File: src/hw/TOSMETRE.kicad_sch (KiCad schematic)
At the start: 61 parts

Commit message: #402
BROULLION
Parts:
- C1, C4: value (none) -> 1µF; footprint (none) -> Capacitor_SMD:C_1206_3216Metric
- C10, C13, C16, C3, C8: value (none) -> 100nF; footprint (none) -> Capacitor_SMD:C_1206_3216Metric
- C11: value (none) -> 2.2µF; footprint (none) -> Capacitor_SMD:C_1206_3216Metric
- C12, C5: value (none) -> 47nF; footprint (none) -> Capacitor_SMD:C_1206_3216Metric
- C14, C17, C2, C7, C9: value (none) -> 10µF; footprint (none) -> Capacitor_SMD:C_1206_3216Metric
- C15, C18: value (none) -> 2nF; footprint (none) -> Capacitor_SMD:C_1206_3216Metric
- C19, C20, C21, C22: value (none) -> NM; footprint (none) -> Capacitor_SMD:C_1206_3216Metric
- C6: value (none) -> 10nF; footprint (none) -> Capacitor_SMD:C_1206_3216Metric
- D1: value (none) -> D; footprint (none) -> Diode_SMD:D_1206_3216Metric
- D2, D3, D4, D5: value (none) -> BAT54XV2; footprint (none) -> Diode_SMD:D_SOD-523
- J1: value (none) -> Barrel_Jack_Switch; footprint (none) -> Connector_PinHeader_2.54mm:PinHeader_1x03_P2.54mm_Vertical_SMD_Pin1Left
- J2, J6: value (none) -> Conn_01x02_Male; footprint (none) -> Connector_PinHeader_2.54mm:PinHeader_1x02_P2.54mm_Vertical_SMD_Pin1Left
- J3: value (none) -> Conn_01x08_Male; footprint (none) -> Connector_PinHeader_2.54mm:PinHeader_1x08_P2.54mm_Vertical_SMD_Pin1Right
- J4: value (none) -> Conn_Coaxial; footprint (none) -> Connector_Coaxial:MMCX_Molex_73415-0961_Horizontal_0.8mm-PCB
- L1, L2: value (none) -> L_Small; footprint (none) -> Resistor_SMD:R_1206_3216Metric
- R11, R4: value (none) -> 4.7K; footprint (none) -> Resistor_SMD:R_1206_3216Metric
- R12, R13, R6, R7: value (none) -> 4.7k; footprint (none) -> Resistor_SMD:R_1206_3216Metric
- R14, R8: value (none) -> 100; footprint (none) -> Resistor_SMD:R_1206_3216Metric
- R15, R9: value (none) -> 1k; footprint (none) -> Resistor_SMD:R_1206_3216Metric
- R16, R17: value (none) -> 50; footprint (none) -> Resistor_SMD:R_1206_3216Metric
- R18, R19, R2, R20, R21, R5: value (none) -> R; footprint (none) -> Resistor_SMD:R_1206_3216Metric
- R3: value (none) -> 10K; footprint (none) -> Resistor_SMD:R_1206_3216Metric
- SW1: value (none) -> SW_DIP_x01; footprint (none) -> Connector_PinHeader_1.00mm:PinHeader_1x02_P1.00mm_Vertical_SMD_Pin1Left
- U1: value (none) -> TPS70950DBVT; footprint (none) -> Package_TO_SOT_SMD:SOT-23-5
- U2: value (none) -> 18F1320; footprint (none) -> Package_SO:HTSSOP-20-1EP_4.4x6.5mm_P0.65mm_EP2.85x4mm
- U3, U5: value (none) -> LT1818; footprint (none) -> Package_TO_SOT_SMD:TSOT-23-5
- U4: value (none) -> LTC2305; footprint (none) -> Package_SO:MSOP-8_3x3mm_P0.65mm

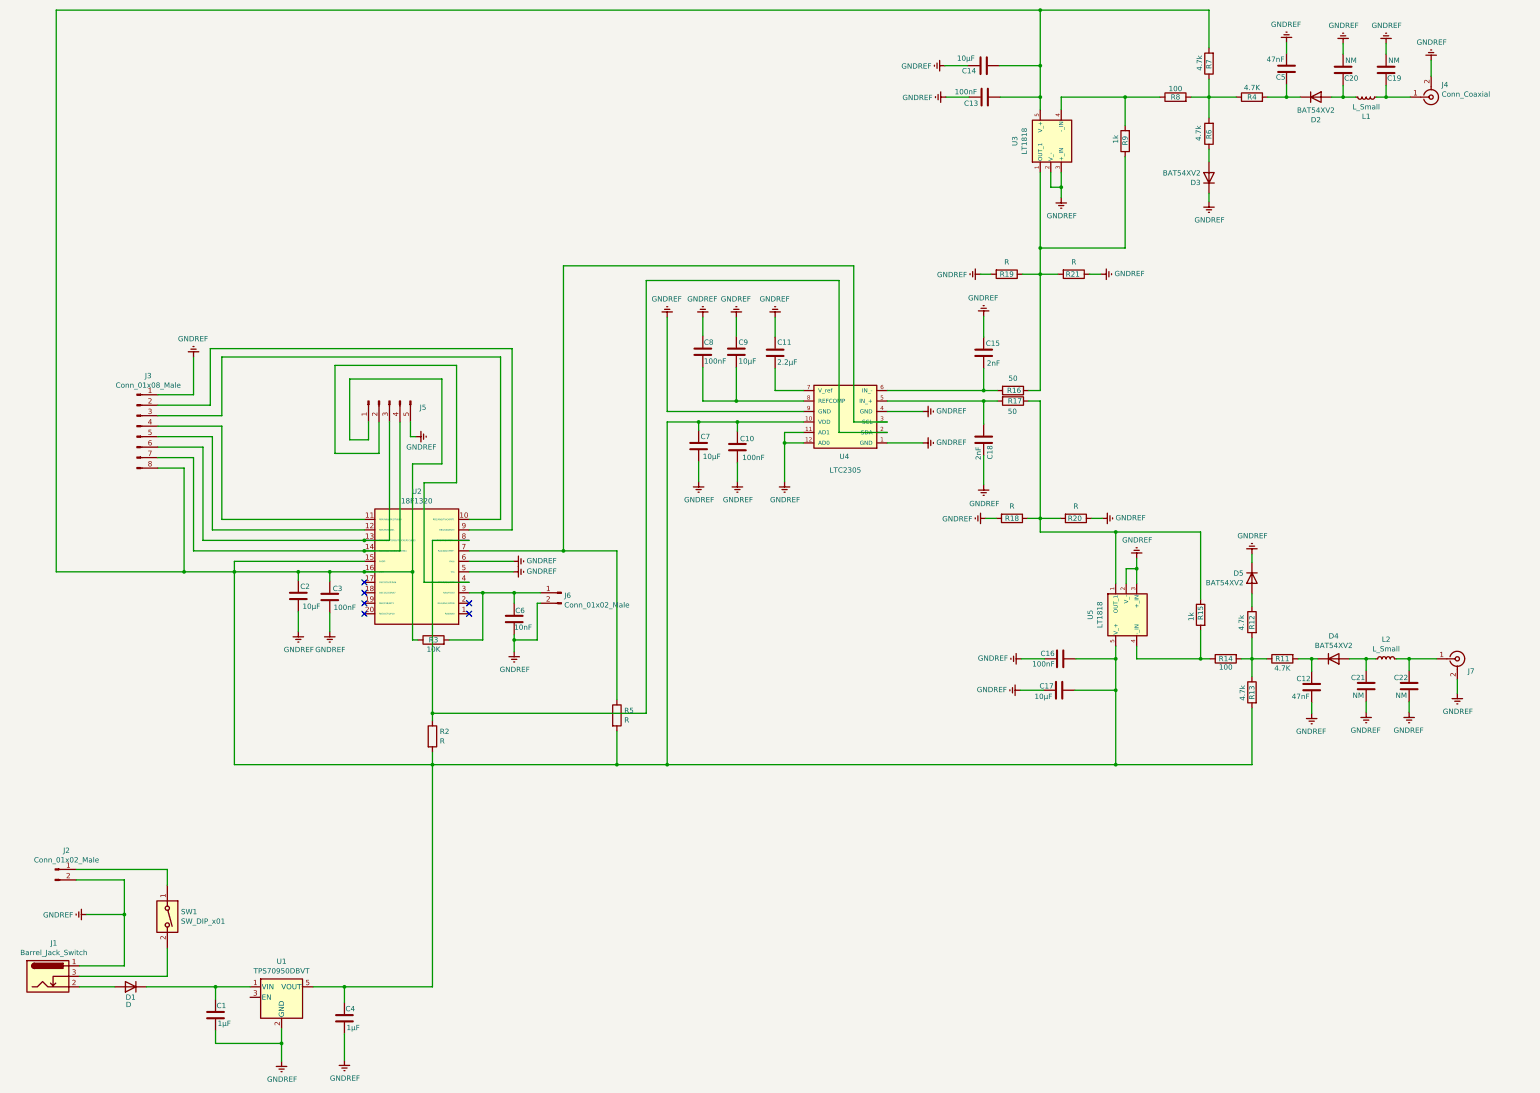
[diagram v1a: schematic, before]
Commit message: #406
pour verification 18F1320 sans pave
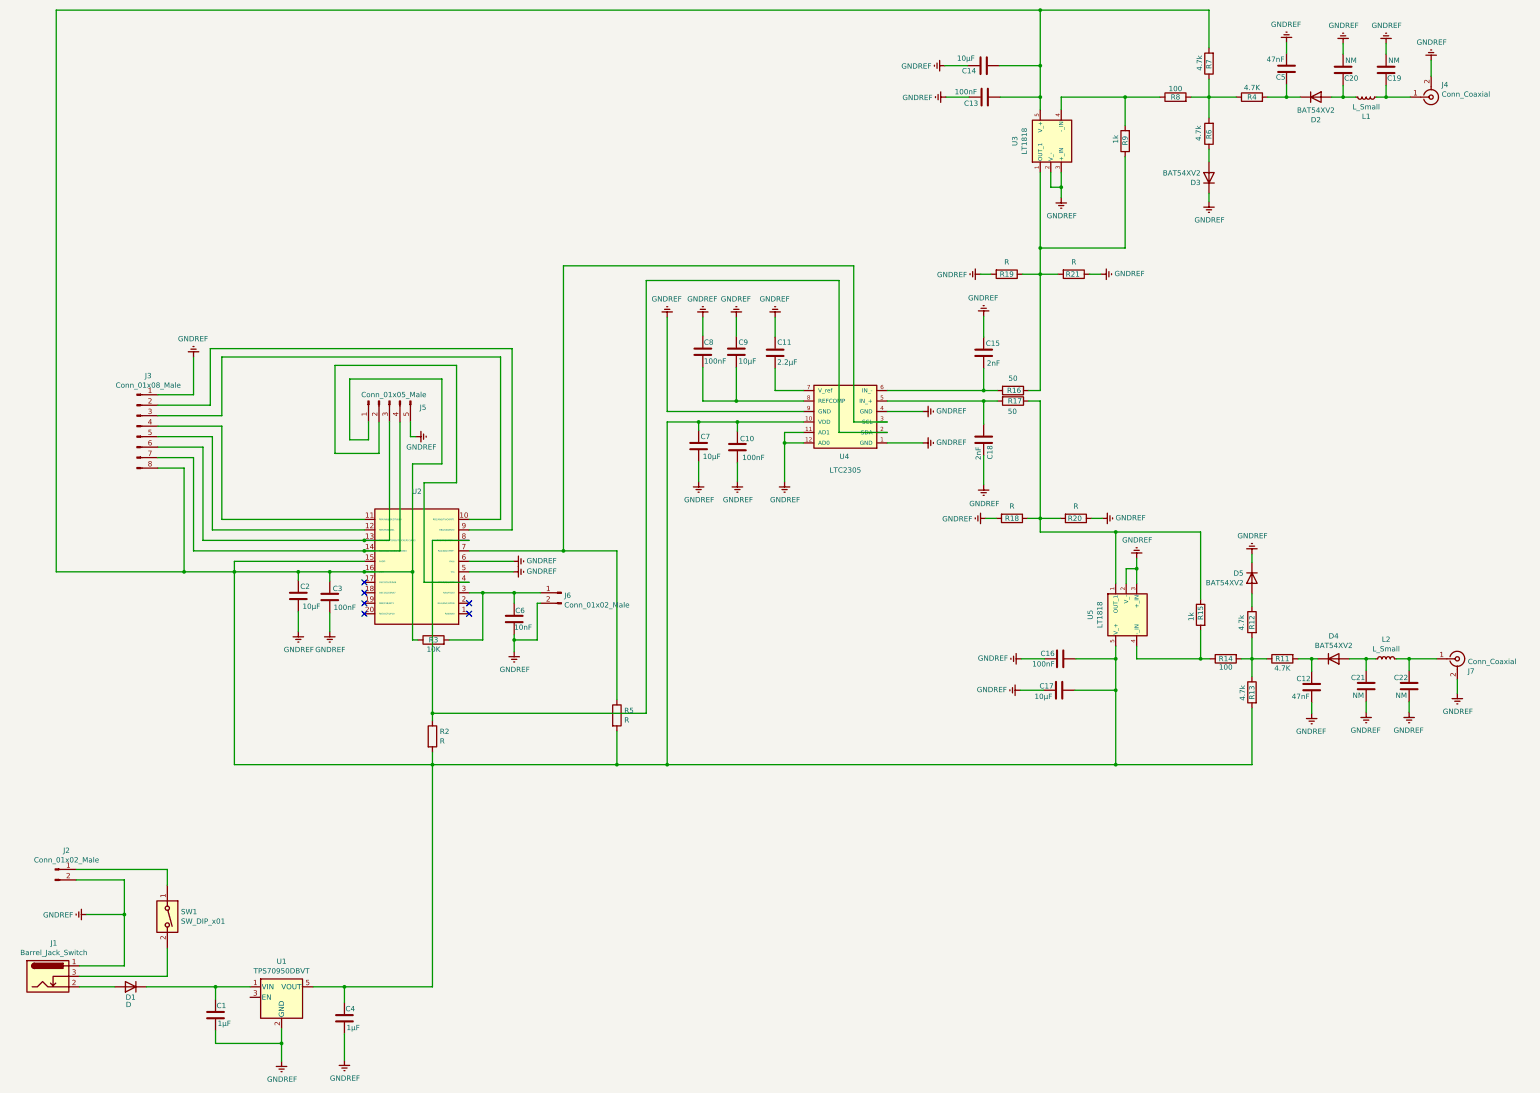
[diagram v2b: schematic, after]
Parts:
- J5: value (none) -> Conn_01x05_Male; footprint (none) -> Connector_PinHeader_2.54mm:PinHeader_1x05_P2.54mm_Vertical_SMD_Pin1Left
- J7: value (none) -> Conn_Coaxial; footprint (none) -> Connector_Coaxial:MMCX_Molex_73415-0961_Horizontal_0.8mm-PCB
- U2: value 18F1320 -> (none); footprint Package_SO:HTSSOP-20-1EP_4.4x6.5mm_P0.65mm_EP2.85x4mm -> (none)
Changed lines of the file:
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@@
-    (stroke (width 0) (type default) (color 0 0 0 0))
-  )
-  (wire (pts (xy 289.56 38.608) (xy 289.56 35.56))
     (stroke (width 0) (type default) (color 0 0 0 0))
   )
@@
     (stroke (width 0) (type default) (color 0 0 0 0))
   )
+  (wire (pts (xy 289.56 35.56) (xy 289.56 38.608))
+    (stroke (width 0) (type default) (color 0 0 0 0))
+  )
   (wire (pts (xy 298.196 171.704) (xy 307.848 171.704))
     (stroke (width 0) (type default) (color 0 0 0 0))
@@
     (in_bom yes) (on_board yes)
     (property "Reference" "U2" (id 0) (at 138.43 131.1402 0))
-    (property "Value" "18F1320" (id 1) (at 138.43 133.4516 0))
-    (property "Footprint" "Package_SO:HTSSOP-20-1EP_4.4x6.5mm_P0.65mm_EP2.85x4mm" (id 2) (at 175.26 143.002 0)
+    (property "Value" "" (id 1) (at 138.43 133.4516 0))
+    (property "Footprint" "" (id 2) (at 175.26 143.002 0)
       (effects (font (size 1.27 1.27)) (justify left) hide)
     )
@@
       (effects (font (size 1.27 1.27)) (justify right))
     )
-    (property "Value" "" (id 1) (at 124.968 107.696 90)
+    (property "Value" "Conn_01x05_Male" (id 1) (at 124.968 107.696 90)
       (effects (font (size 1.27 1.27)) (justify right))
     )
-    (property "Footprint" "" (id 2) (at 131.826 109.22 0)
+    (property "Footprint" "Connector_PinHeader_2.54mm:PinHeader_1x05_P2.54mm_Vertical_SMD_Pin1Left" (id 2) (at 131.826 109.22 0)
       (effects (font (size 1.27 1.27)) hide)
     )
@@
       (effects (font (size 1.27 1.27)) (justify left))
     )
-    (property "Value" "" (id 1) (at 393.192 172.3898 0)
-      (effects (font (size 1.27 1.27)) (justify left))
-    )
-    (property "Footprint" "" (id 2) (at 390.652 171.704 0)
+    (property "Value" "Conn_Coaxial" (id 1) (at 393.192 172.3898 0)
+      (effects (font (size 1.27 1.27)) (justify left))
+    )
+    (property "Footprint" "Connector_Coaxial:MMCX_Molex_73415-0961_Horizontal_0.8mm-PCB" (id 2) (at 390.652 171.704 0)
       (effects (font (size 1.27 1.27)) hide)
     )
@@
     )
     (path "/00000000-0000-0000-0000-000060439842"
-      (reference "U2") (unit 1) (value "18F1320") (footprint "Package_SO:HTSSOP-20-1EP_4.4x6.5mm_P0.65mm_EP2.85x4mm")
+      (reference "U2") (unit 1) (value "18F1320") (footprint "Package_SO:SSOP-20_4.4x6.5mm_P0.65mm")
     )
     (path "/00000000-0000-0000-0000-00006043d9b3"

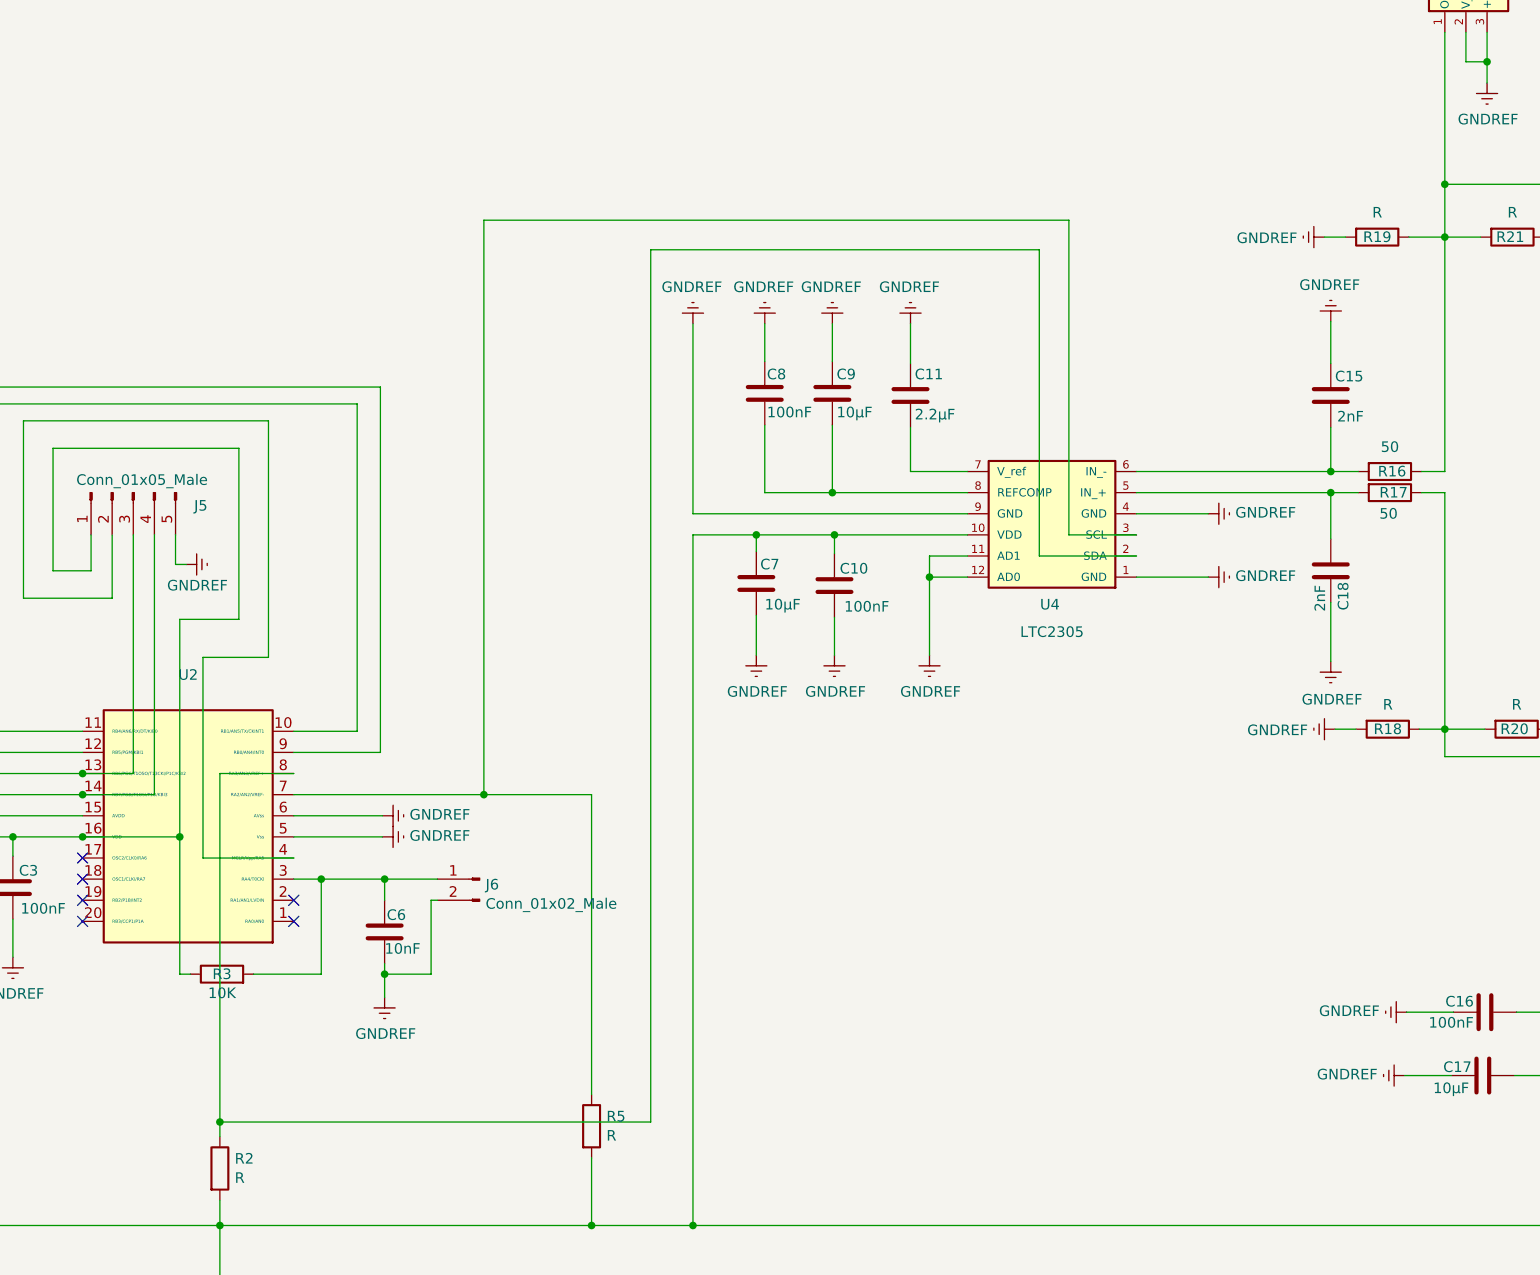
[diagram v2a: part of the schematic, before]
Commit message: #406
modification piste qui se croise sous U2
A valider  par PANORAMIX
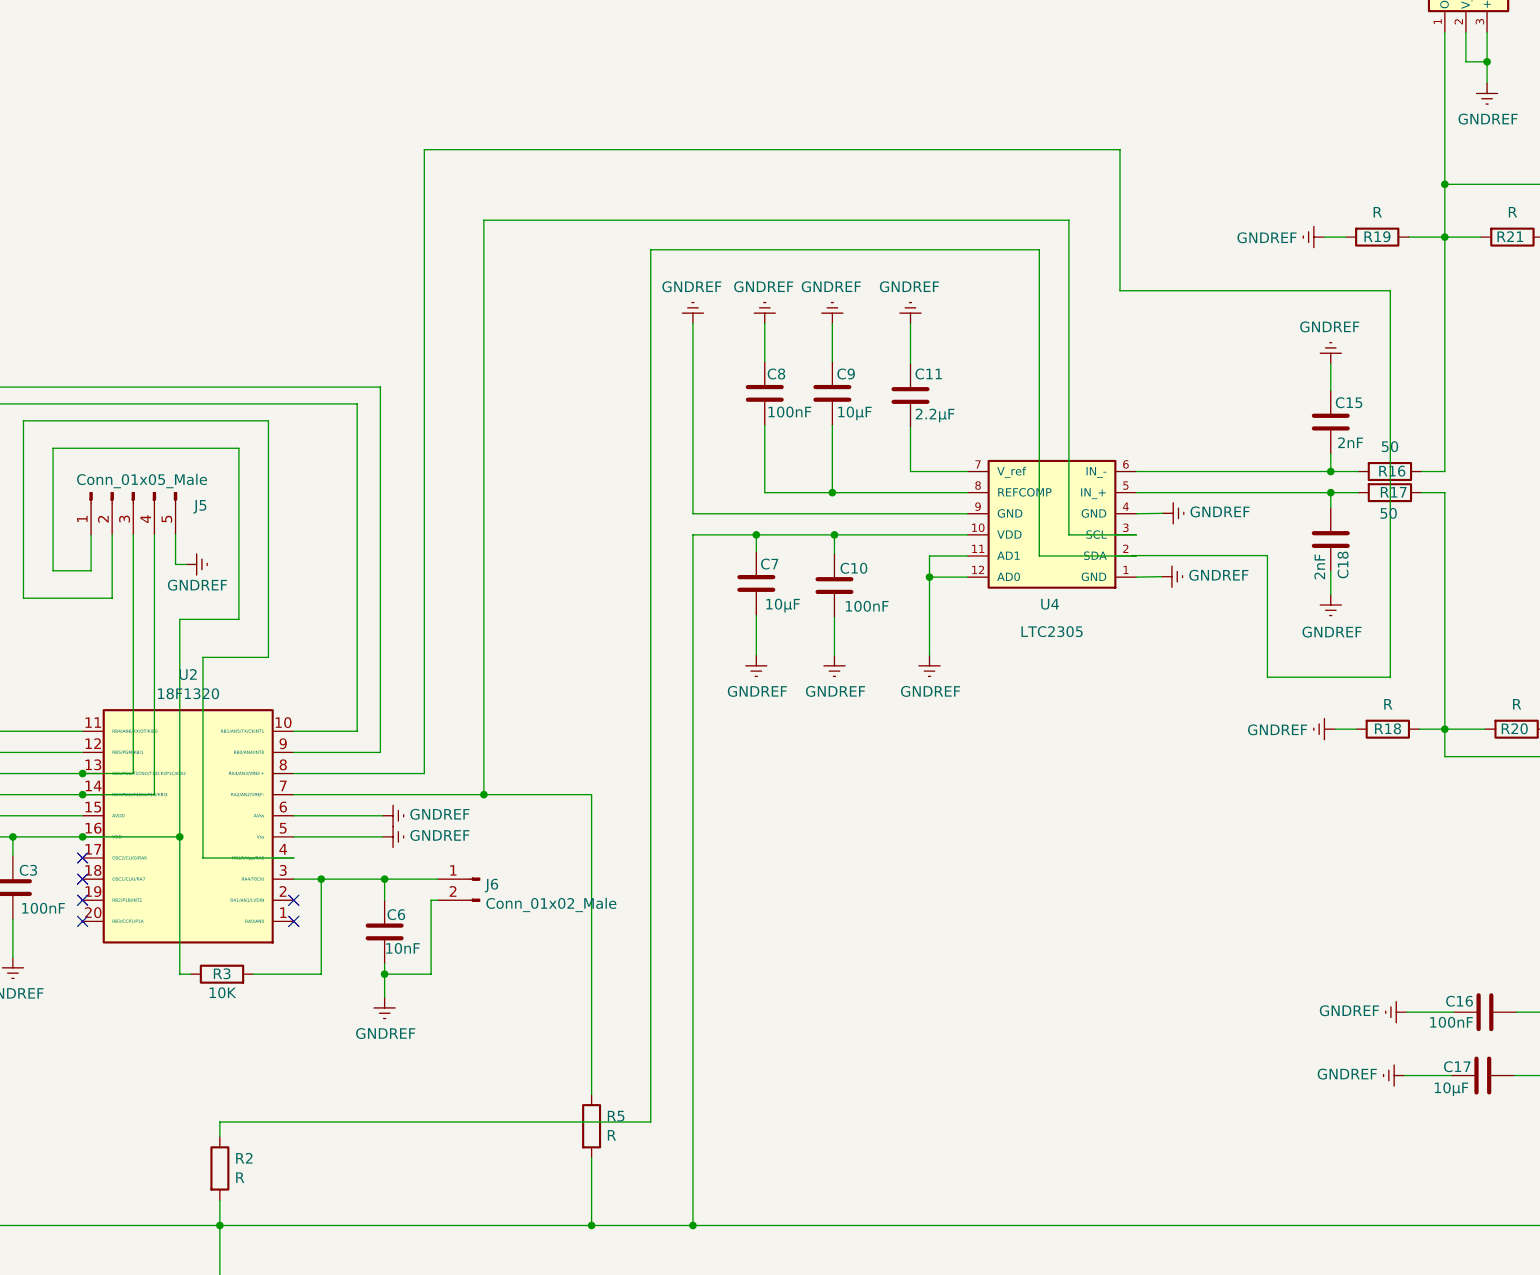
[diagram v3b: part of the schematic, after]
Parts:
- U2: value (none) -> 18F1320; footprint (none) -> Package_SO:SSOP-20_4.4x6.5mm_P0.65mm
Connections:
- net at R2.1, U4.2 (SDA): no longer U2.8 (RA3/AN3/VREF+)
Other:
- moved on the sheet: C15, C18
